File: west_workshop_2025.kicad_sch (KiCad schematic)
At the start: 6 parts, among them SW1 switch_1.00u

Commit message: Cleaned schematic --blank--
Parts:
- removed SW1: switch_1.00u, 0_west_footprints:SW_Cherry_MX_PCB_1.00u, symbol 0_west_symbols:Switch_Push
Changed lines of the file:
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@@
-	)
-	(symbol
-		(lib_id "0_west_symbols:Switch_Push")
-		(at 193.04 133.35 0)
-		(unit 1)
-		(exclude_from_sim no)
-		(in_bom yes)
-		(on_board yes)
-		(dnp no)
-		(fields_autoplaced yes)
-		(property "Reference" "SW1"
-			(at 193.04 128.27 0)
-			(effects
-				(font
-					(size 1.27 1.27)
-				)
-			)
-		)
-		(property "Value" "switch_1.00u"
-			(at 193.04 134.874 0)
-			(effects
-				(font
-					(size 1.27 1.27)
-				)
-				(hide yes)
-			)
-		)
-		(property "Footprint" "0_west_footprints:SW_Cherry_MX_PCB_1.00u"
-			(at 193.04 128.27 0)
-			(effects
-				(font
-					(size 1.27 1.27)
-				)
-				(hide yes)
-			)
-		)
-		(property "Datasheet" "~"
-			(at 193.04 128.27 0)
-			(effects
-				(font
-					(size 1.27 1.27)
-				)
-				(hide yes)
-			)
-		)
-		(property "Description" "Push button switch, Cherry_MX_PCB_1.00u, Soldered"
-			(at 193.04 133.35 0)
-			(effects
-				(font
-					(size 1.27 1.27)
-				)
-				(hide yes)
-			)
-		)
-		(pin "1"
-		)
-		(pin "2"
-		)
-		(instances
-			(project ""
-				(path "/baeebffa-96bb-43bb-bf83-a06dcef072ea"
-					(reference "SW1")
-					(unit 1)
-				)
-			)
-		)
 	)
 	(symbol

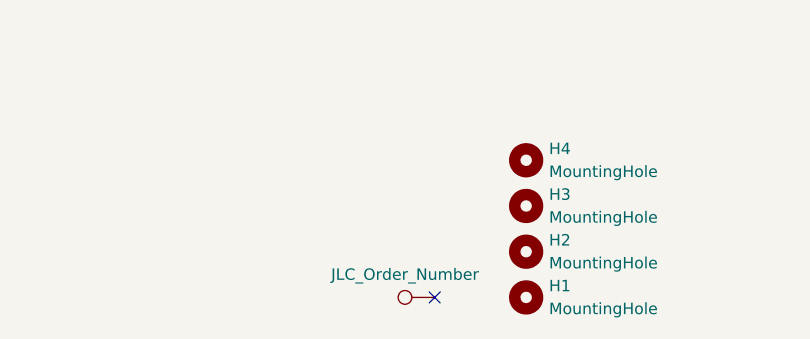
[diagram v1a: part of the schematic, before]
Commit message: Added more notes, Removed JLC footprint TP
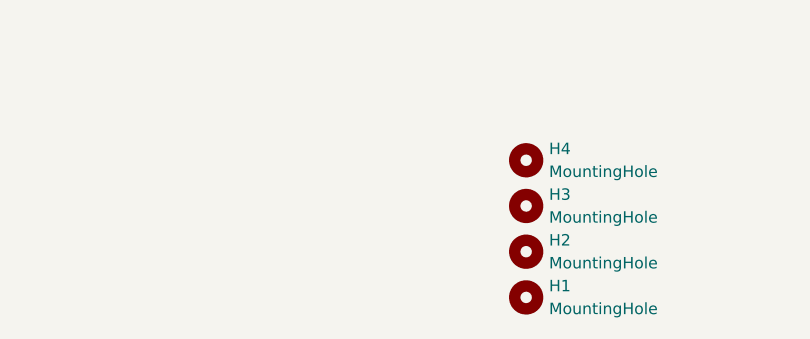
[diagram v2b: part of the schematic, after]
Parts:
- removed TP1: JLC_Order_Number, west_footprints:JLC_Order_Number, symbol Connector:TestPoint
- H1, H2, H3, H4: footprint west_footprints:MountingHole_M2 -> 0_west_footprints:MountingHole_M2
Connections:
- no-connect marks 1 -> 0
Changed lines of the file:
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@@
-		)
-	)
-	(no_connect
-		(at 147.32 190.5)
-	)
-	(symbol
-		(lib_id "Connector:TestPoint")
-		(at 147.32 190.5 90)
-		(unit 1)
-		(exclude_from_sim no)
-		(in_bom yes)
-		(on_board yes)
-		(dnp no)
-		(fields_autoplaced yes)
-		(property "Reference" "TP1"
-			(at 144.018 185.42 90)
-			(effects
-				(font
-					(size 1.27 1.27)
-				)
-				(hide yes)
-			)
-		)
-		(property "Value" "JLC_Order_Number"
-			(at 144.018 187.96 90)
-			(effects
-				(font
-					(size 1.27 1.27)
-				)
-			)
-		)
-		(property "Footprint" "west_footprints:JLC_Order_Number"
-			(at 147.32 185.42 0)
-			(effects
-				(font
-					(size 1.27 1.27)
-				)
-				(hide yes)
-			)
-		)
-		(property "Datasheet" "~"
-			(at 147.32 185.42 0)
-			(effects
-				(font
-					(size 1.27 1.27)
-				)
-				(hide yes)
-			)
-		)
-		(property "Description" "test point"
-			(at 147.32 190.5 0)
-			(effects
-				(font
-					(size 1.27 1.27)
-				)
-				(hide yes)
-			)
-		)
-		(pin "1"
-		)
-		(instances
-			(project ""
-				(path "/baeebffa-96bb-43bb-bf83-a06dcef072ea"
-					(reference "TP1")
-					(unit 1)
-				)
-			)
 		)
 	)
@@
 			)
 		)
-		(property "Footprint" "west_footprints:MountingHole_M2"
+		(property "Footprint" "0_west_footprints:MountingHole_M2"
 			(at 157.48 185.42 0)
 			(effects
@@
 			)
 		)
-		(property "Footprint" "west_footprints:MountingHole_M2"
+		(property "Footprint" "0_west_footprints:MountingHole_M2"
 			(at 157.48 190.5 0)
 			(effects
@@
 			)
 		)
-		(property "Footprint" "west_footprints:MountingHole_M2"
+		(property "Footprint" "0_west_footprints:MountingHole_M2"
 			(at 157.48 175.26 0)
 			(effects
@@
 			)
 		)
-		(property "Footprint" "west_footprints:MountingHole_M2"
+		(property "Footprint" "0_west_footprints:MountingHole_M2"
 			(at 157.48 180.34 0)
 			(effects
